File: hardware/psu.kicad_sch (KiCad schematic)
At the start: 36 parts, among them J1 12V Barrel, J2 12V Screw Terminal, Q1 FDS4435BZ, U1 NCP1117-3.3_SOT223, U2 AP64501SP-13

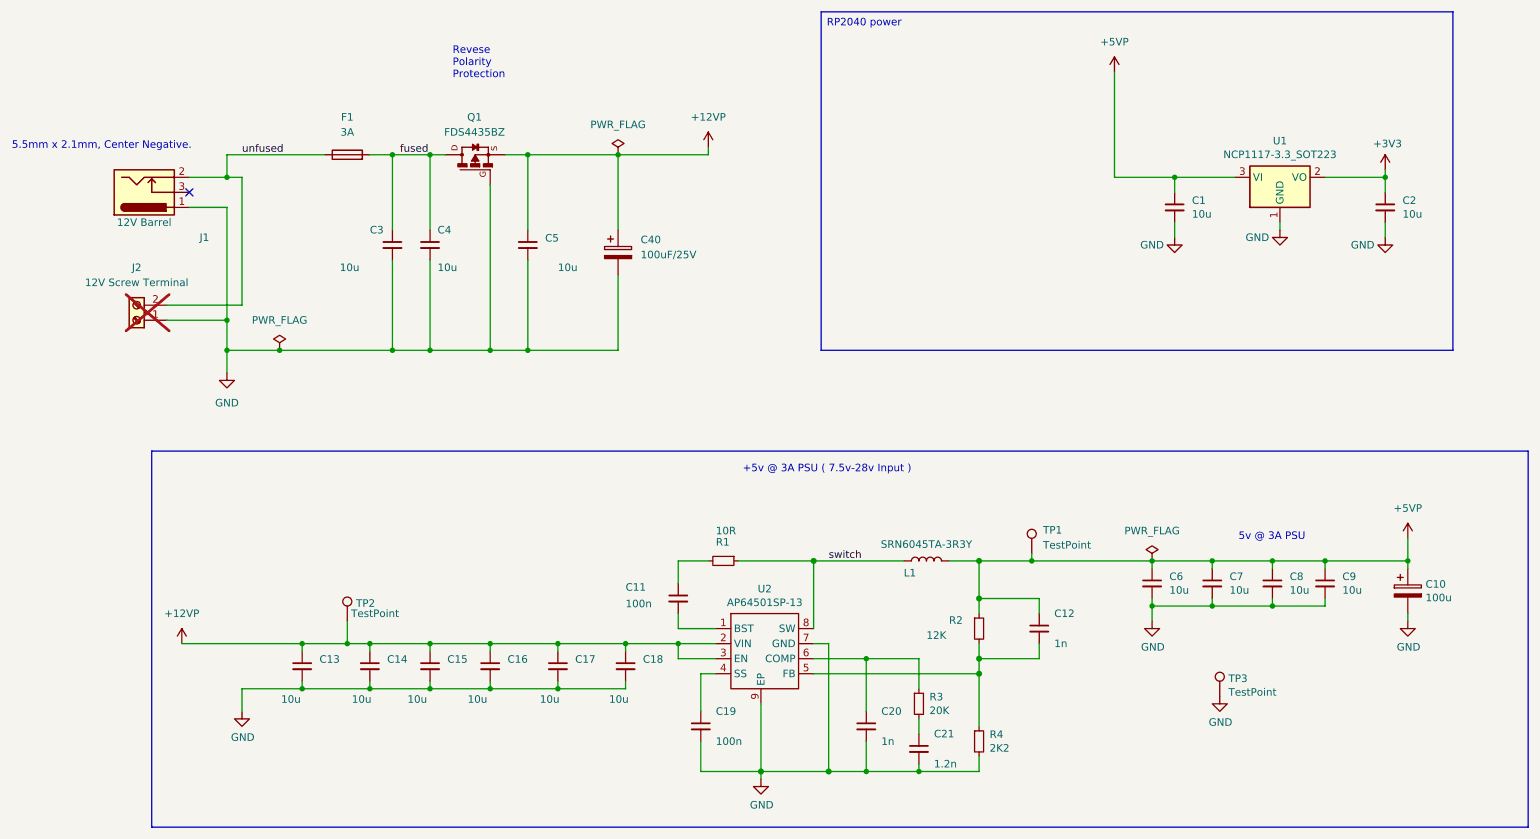
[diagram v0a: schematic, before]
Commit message: refactor: reannotate PCB by position + rename IC1 to U prefix
All reference designators renumbered top-to-bottom, left-to-right.
ASM1061 changed from IC to U prefix.
ERC: 0 errors. DRC: 0 violations. Parity: 0 issues.
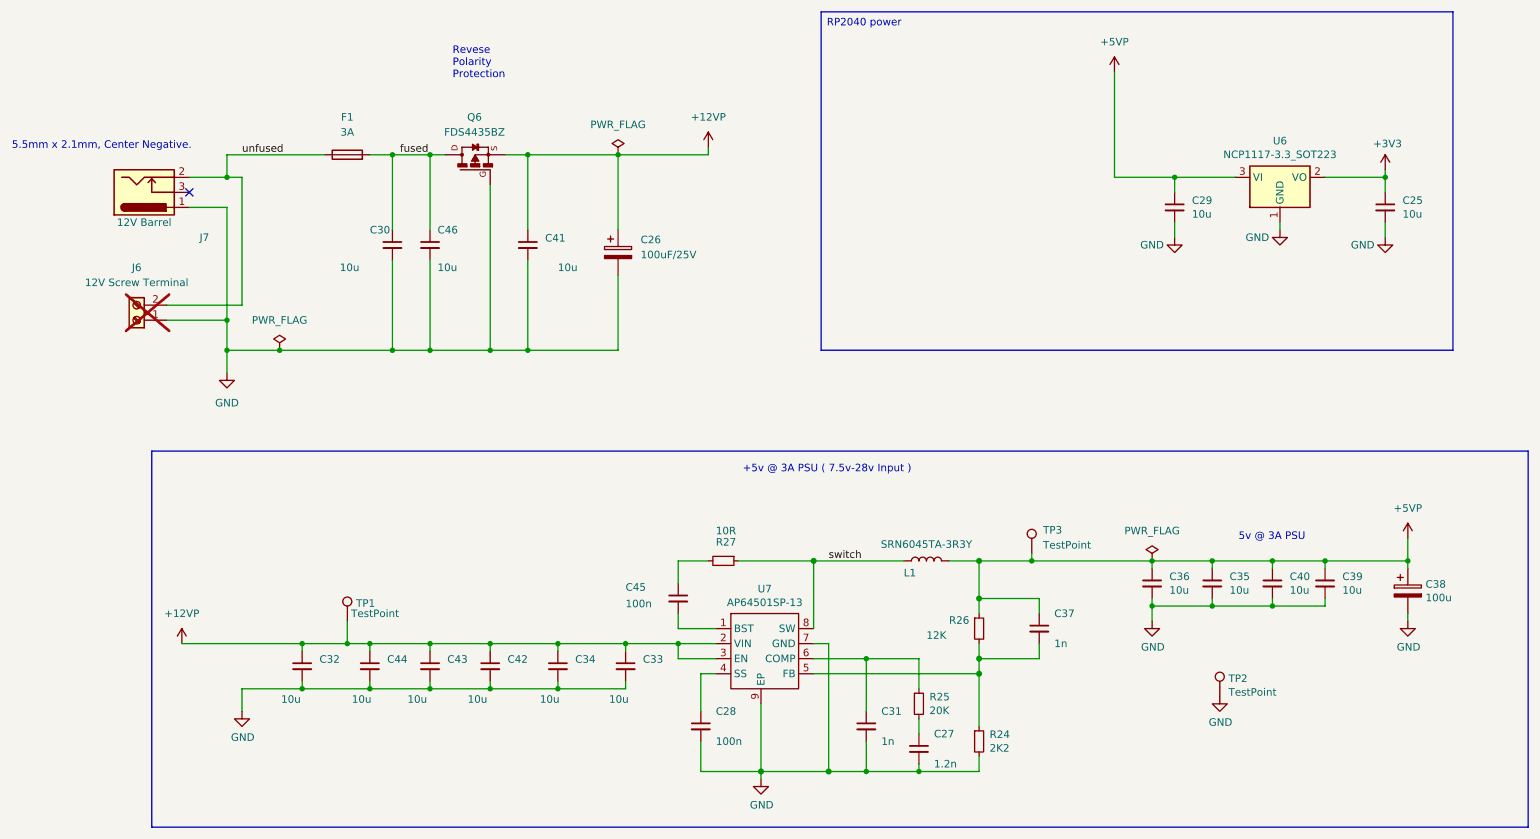
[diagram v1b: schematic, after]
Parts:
- C25: renamed from C2; KiLib_Generator (none) -> SMD_2terminal_chip_molded
- C26: renamed from C40; KiLib_Generator (none) -> capacitor/SMD/elec_round_polarized
- C27: renamed from C21; KiLib_Generator (none) -> SMD_2terminal_chip_molded
- C28: renamed from C19; KiLib_Generator (none) -> SMD_2terminal_chip_molded
- C29: renamed from C1; KiLib_Generator (none) -> SMD_2terminal_chip_molded
- C30: renamed from C3; KiLib_Generator (none) -> SMD_2terminal_chip_molded
- C31: renamed from C20; KiLib_Generator (none) -> SMD_2terminal_chip_molded
- C32: renamed from C13; KiLib_Generator (none) -> SMD_2terminal_chip_molded
- C33: renamed from C18; KiLib_Generator (none) -> SMD_2terminal_chip_molded
- C34: renamed from C17; KiLib_Generator (none) -> SMD_2terminal_chip_molded
- C35: renamed from C7; KiLib_Generator (none) -> SMD_2terminal_chip_molded
- C36: renamed from C6; KiLib_Generator (none) -> SMD_2terminal_chip_molded
- C37: renamed from C12; KiLib_Generator (none) -> SMD_2terminal_chip_molded
- C38: renamed from C10; KiLib_Generator (none) -> SMD_2terminal_chip_molded
- C39: renamed from C9; KiLib_Generator (none) -> SMD_2terminal_chip_molded
- C40: renamed from C8; KiLib_Generator (none) -> SMD_2terminal_chip_molded
- C41: renamed from C5; KiLib_Generator (none) -> SMD_2terminal_chip_molded
- C42: renamed from C16; KiLib_Generator (none) -> SMD_2terminal_chip_molded
- C43: renamed from C15; KiLib_Generator (none) -> SMD_2terminal_chip_molded
- C44: renamed from C14; KiLib_Generator (none) -> SMD_2terminal_chip_molded
- C45: renamed from C11; KiLib_Generator (none) -> SMD_2terminal_chip_molded
- C46: renamed from C4; KiLib_Generator (none) -> SMD_2terminal_chip_molded
- F1: KiLib_Generator (none) -> SMD_2terminal_chip_molded
- J6: renamed from J2; KiLib_Generator (none) -> terminal_block/Phoenix
- R24: renamed from R4; KiLib_Generator (none) -> SMD_2terminal_chip_molded
- R25: renamed from R3; KiLib_Generator (none) -> SMD_2terminal_chip_molded
- R26: renamed from R2; KiLib_Generator (none) -> SMD_2terminal_chip_molded
- R27: renamed from R1; KiLib_Generator (none) -> SMD_2terminal_chip_molded
- renumbered J1 to J7, Q1 to Q6, TP2 to TP1, TP3 to TP2, TP1 to TP3, U1 to U6, U2 to U7
